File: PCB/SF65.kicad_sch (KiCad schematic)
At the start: 176 parts, among them J1 C165948_-_USB_C_Receptacle_US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, J2 SM02B-SRSS-TB(LF)(SN), Q1 Q_PMOS_GSD, SW1 CAP_STP, SW10 A, SW11 WIN_1.25U, SW12 2, SW13 W, SW14 S, SW15 Z, SW16 L_ALT_1.25U, SW17 L_ALT_1.5U, SW18 3, SW19 E, SW2 ESC, SW20 D, SW21 X, SW22 4, SW23 R, SW24 F, SW25 C, SW26 5, SW27 T, SW28 G, SW29 V, SW3 Tab, SW30 SPC_6.25U, SW31 SPC_7U, SW32 6, SW33 Y, SW34 H, SW35 B, SW36 7, SW37 U, SW38 J, SW39 N, SW4 CAP, SW40 8, SW41 I, SW42 K, SW43 M, SW44 R_ALT_1U, SW45 R_ALT_1.5U, SW46 9, SW47 O, SW48 L, SW49 ,, SW5 L_SHFT, SW50 R_WIN_1U, SW51 R_CTRL_1.5U, SW52 0, SW53 P, SW54 ;, SW55 ., SW56 R_CTRL_1U, SW57 -, SW58 [, SW59 ', SW6 L_CTRL_1.25U, SW60 /, SW61 =, SW62 ], SW63 R_SHFT_1.75U, SW64 LEFT, SW65 R_SHFT_1.5U, SW66 BCKSP, SW67 \, SW68 ENT, SW69 UP, SW7 L_CTRL_1.5U, SW70 DOWN, SW71 ENT_ISO, SW72 Tilde, SW73 Del, SW74 PG_UP, SW75 PG_DWN, SW76 RIGHT, SW8 1, SW9 Q, U1 TP4054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

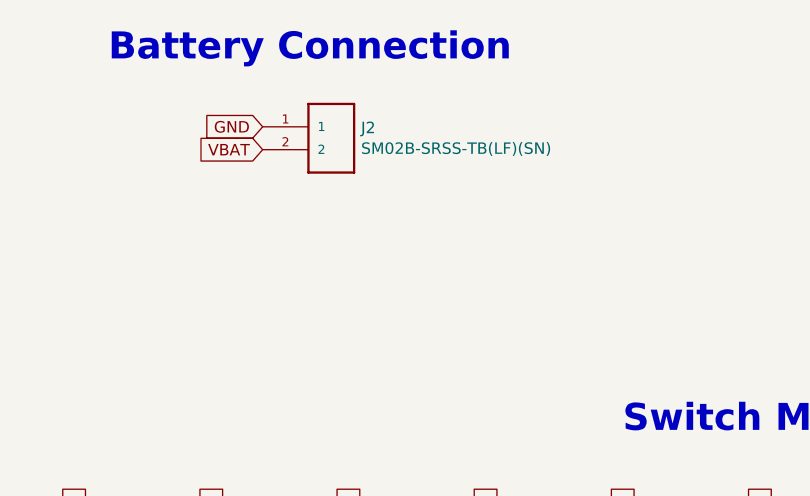
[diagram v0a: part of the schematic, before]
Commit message: working on routing, not complete
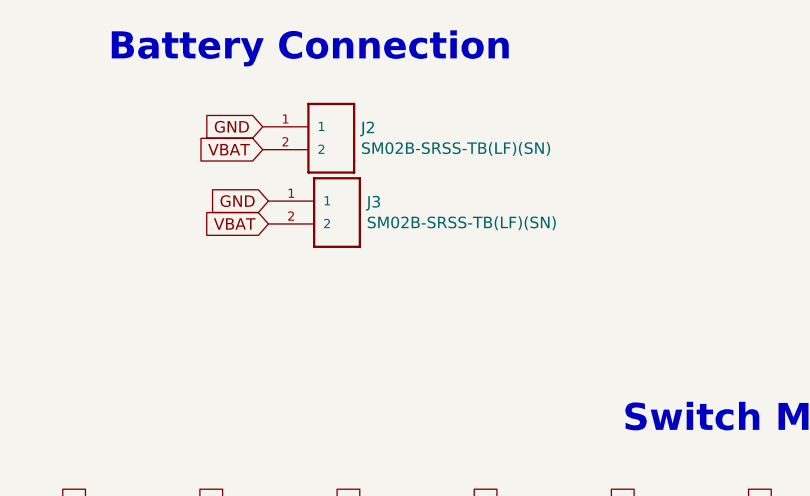
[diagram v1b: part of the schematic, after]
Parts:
- added J3: SM02B-SRSS-TB(LF)(SN), Connector_PinHeader_2.54mm:PinHeader_1x02_P2.54mm_Vertical, symbol SM02B-SRSS-TB_LF__SN_:SM02B-SRSS-TB(LF)(SN)
- H1, H2, H3, H4, H5, H6: footprint MountingHole:MountingHole_4.3mm_M4 -> MountingHole:MountingHole_2.2mm_M2
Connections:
- net GND: now also J3.1
- net VBAT: now also J3.2
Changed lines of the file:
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@@
+    (effects (font (size 1.27 1.27)) (justify right))
+  )
+  (global_label "GND" (shape input) (at 97.79 -5.08 180)    (property "Intersheet References" "${INTERSHEET_REFS}" (id 0) (at -396.24 -186.69 0)
+      (effects (font (size 1.27 1.27)) hide)
+    )
+    (effects (font (size 1.27 1.27)) (justify right))
+  )
+  (global_label "VBAT" (shape input) (at 97.79 -2.54 180)    (property "Intersheet References" "${INTERSHEET_REFS}" (id 0) (at -396.24 -181.61 0)
+      (effects (font (size 1.27 1.27)) hide)
+    )
     (effects (font (size 1.27 1.27)) (justify right))
   )
@@
       (effects (font (size 1.27 1.27)) (justify left))
     )
-    (property "Footprint" "MountingHole:MountingHole_4.3mm_M4" (id 2) (at -31.75 59.69 0)
+    (property "Footprint" "MountingHole:MountingHole_2.2mm_M2" (id 2) (at -31.75 59.69 0)
       (effects (font (size 1.27 1.27)) hide)
     )
@@
       (effects (font (size 1.27 1.27)) (justify left))
     )
-    (property "Footprint" "MountingHole:MountingHole_4.3mm_M4" (id 2) (at -31.75 67.31 0)
+    (property "Footprint" "MountingHole:MountingHole_2.2mm_M2" (id 2) (at -31.75 67.31 0)
       (effects (font (size 1.27 1.27)) hide)
     )
@@
       (effects (font (size 1.27 1.27)) (justify left))
     )
-    (property "Footprint" "MountingHole:MountingHole_4.3mm_M4" (id 2) (at -31.75 74.93 0)
+    (property "Footprint" "MountingHole:MountingHole_2.2mm_M2" (id 2) (at -31.75 74.93 0)
       (effects (font (size 1.27 1.27)) hide)
     )
@@
       (effects (font (size 1.27 1.27)) (justify left))
     )
-    (property "Footprint" "MountingHole:MountingHole_4.3mm_M4" (id 2) (at -31.75 82.55 0)
+    (property "Footprint" "MountingHole:MountingHole_2.2mm_M2" (id 2) (at -31.75 82.55 0)
       (effects (font (size 1.27 1.27)) hide)
     )
@@
       (effects (font (size 1.27 1.27)) (justify left))
     )
-    (property "Footprint" "MountingHole:MountingHole_4.3mm_M4" (id 2) (at -31.75 90.17 0)
+    (property "Footprint" "MountingHole:MountingHole_2.2mm_M2" (id 2) (at -31.75 90.17 0)
       (effects (font (size 1.27 1.27)) hide)
     )
@@
       (effects (font (size 1.27 1.27)) (justify left))
     )
-    (property "Footprint" "MountingHole:MountingHole_4.3mm_M4" (id 2) (at -31.75 97.79 0)
+    (property "Footprint" "MountingHole:MountingHole_2.2mm_M2" (id 2) (at -31.75 97.79 0)
       (effects (font (size 1.27 1.27)) hide)
     )
@@
     )
   )
+  (symbol (lib_id "SM02B-SRSS-TB_LF__SN_:SM02B-SRSS-TB(LF)(SN)") (at 97.79 0 0) (unit 1)
+    (in_bom yes) (on_board yes)
+    (property "Reference" "J3" (id 0) (at 108.7121 -4.9594 0)
+      (effects (font (size 1.27 1.27)) (justify left))
+    )
+    (property "Value" "SM02B-SRSS-TB(LF)(SN)" (id 1) (at 108.7121 -2.6607 0)
+      (effects (font (size 1.27 1.27)) (justify left))
+    )
+    (property "Footprint" "Connector_PinHeader_2.54mm:PinHeader_1x02_P2.54mm_Vertical" (id 2) (at 97.79 0 0)
+      (effects (font (size 1.27 1.27)) (justify left bottom) hide)
+    )
+    (property "Datasheet" "" (id 3) (at 97.79 0 0)
+      (effects (font (size 1.27 1.27)) (justify left bottom) hide)
+    )
+    (property "MP" "SM02B-SRSS-TB_LF__SN_" (id 4) (at 97.79 0 0)
+      (effects (font (size 1.27 1.27)) (justify left bottom) hide)
+    )
+    (property "AVAILABILITY" "Good" (id 5) (at 97.79 0 0)
+      (effects (font (size 1.27 1.27)) (justify left bottom) hide)
+    )
+    (property "PRICE" "0.23 USD" (id 6) (at 97.79 0 0)
+      (effects (font (size 1.27 1.27)) (justify left bottom) hide)
+    )
+    (property "DESCRIPTION" "SH Series 2 Position 1 mm Pitch Surface Mount Side Entry Shrouded Header" (id 7) (at 97.79 0 0)
+      (effects (font (size 1.27 1.27)) (justify left bottom) hide)
+    )
+    (property "MF" "JST" (id 8) (at 97.79 0 0)
+      (effects (font (size 1.27 1.27)) (justify left bottom) hide)
+    )
+    (property "PACKAGE" "None" (id 9) (at 97.79 0 0)
+      (effects (font (size 1.27 1.27)) (justify left bottom) hide)
+    )
+  )
   (symbol (lib_id "COBoards:Q_PMOS_GSD") (at -67.31 208.28 0) (unit 1)
     (in_bom yes) (on_board yes)
@@
     )
     (path "/57c2b6d5-409c-411a-87d5-01c7b443a274"
-      (reference "H1") (unit 1) (value "MountingHole_Pad") (footprint "MountingHole:MountingHole_4.3mm_M4")
+      (reference "H1") (unit 1) (value "MountingHole_Pad") (footprint "MountingHole:MountingHole_2.2mm_M2")
     )
     (path "/e5cfd2fa-2e8d-4059-88e3-68afbd63f1ed"
-      (reference "H2") (unit 1) (value "MountingHole_Pad") (footprint "MountingHole:MountingHole_4.3mm_M4")
+      (reference "H2") (unit 1) (value "MountingHole_Pad") (footprint "MountingHole:MountingHole_2.2mm_M2")
     )
     (path "/7f6e663e-0905-4ac2-9f94-84e0580516c6"
-      (reference "H3") (unit 1) (value "MountingHole_Pad") (footprint "MountingHole:MountingHole_4.3mm_M4")
+      (reference "H3") (unit 1) (value "MountingHole_Pad") (footprint "MountingHole:MountingHole_2.2mm_M2")
     )
     (path "/37c9d4f3-312f-47f1-9f4d-1c07624f0e6c"
-      (reference "H4") (unit 1) (value "MountingHole_Pad") (footprint "MountingHole:MountingHole_4.3mm_M4")
+      (reference "H4") (unit 1) (value "MountingHole_Pad") (footprint "MountingHole:MountingHole_2.2mm_M2")
     )
     (path "/b5d95a24-2753-4eb3-a390-07ddb53afbc0"
-      (reference "H5") (unit 1) (value "MountingHole_Pad") (footprint "MountingHole:MountingHole_4.3mm_M4")
+      (reference "H5") (unit 1) (value "MountingHole_Pad") (footprint "MountingHole:MountingHole_2.2mm_M2")
     )
     (path "/56d59270-8362-4bcd-b006-3b599e0c3d78"
-      (reference "H6") (unit 1) (value "MountingHole_Pad") (footprint "MountingHole:MountingHole_4.3mm_M4")
+      (reference "H6") (unit 1) (value "MountingHole_Pad") (footprint "MountingHole:MountingHole_2.2mm_M2")
     )
     (path "/828ef4a2-7b85-44c5-b8f5-7943f2969d3f"
@@
       (reference "J2") (unit 1) (value "SM02B-SRSS-TB(LF)(SN)") (footprint "COBoards:SM02B-SRSS-TB(LF)(SN)")
     )
+    (path "/70b5bca1-0b96-4ac4-a51e-5aa21489f7ca"
+      (reference "J3") (unit 1) (value "SM02B-SRSS-TB(LF)(SN)") (footprint "Connector_PinHeader_2.54mm:PinHeader_1x02_P2.54mm_Vertical")
+    )
     (path "/740890ae-c843-4a97-b564-35439ebfa574"

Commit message: about to swap in raytac module
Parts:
- added C6, C7: 15pF, Capacitor_SMD:C_0603_1608Metric, symbol Device:C_Small
- added U3: MDBT50Q-1MV2, RF_Module:Raytac_MDBT50Q, symbol RF_Module:MDBT50Q-1MV2
- added Y2: 32.768kHz, COBoards:FC-135R_L3.2-W1.5, symbol Device:Crystal
- C1, C2: value 22pF -> 15pF
- Y1: footprint Crystal:Crystal_SMD_MicroCrystal_CM9V-T1A-2Pin_1.6x1.0mm_HandSoldering -> COBoards:FC-135R_L3.2-W1.5
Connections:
- net BATTERY_MEASURE: now also U3.20 (P0.04/AIN2); no longer BLE1.3 (P0.03/AIN1_(LowFreq))
- net Col0: now also BLE1.2 (P1.10_(LowFreq)), U3.3 (P1.10)
- net Col1: now also BLE1.4 (P0.28/AIN4), U3.4 (P1.11)
- net Col10: now also U3.13 (P0.28/AIN4)
- net Col11: now also U3.14 (P0.30/AIN6)
- net Col12: now also U3.22 (P0.06)
- net Col13: now also U3.24 (P0.08)
- net Col14: now also U3.26 (TRACEDATA3/P1.09)
- net Col2: now also BLE1.6 (P1.13_(LowFreq)), U3.5 (P1.12)
- net Col3: now also U3.6 (P1.13)
- net Col4: now also U3.7 (P1.14)
- net Col5: now also U3.8 (P1.15)
- net Col6: now also U3.9 (P0.03/AIN1)
- net Col7: now also U3.10 (P0.29/AIN5)
- net Col8: now also U3.11 (P0.02/AIN0)
- net Col9: now also U3.12 (P0.31/AIN7)
- net D+: now also U3.35 (D+); no longer BLE1.31 (D+)
- net D-: now also U3.34 (D-); no longer BLE1.29 (D-)
- net GND: now also C6.1, C7.1; no longer BLE1.5 (GND)
- net P0.05: now also U3.50 (P1.02)
- net RESET: now also U3.40 (~RESET~/P0.18); no longer BLE1.26 (P0.18/RESET)
- net Row0: now also BLE1.1 (P1.11), U3.56 (P1.04)
- net Row1: now also U3.57 (P1.06)
- net Row2: now also U3.58 (P1.07)
- net Row3: now also U3.59 (P1.05)
- net Row4: now also U3.60 (P1.03)
- net SWC: now also U3.53 (SWDCLK); no longer BLE1.39 (SWDCLK)
- net SWD: now also U3.51 (SWDIO); no longer BLE1.37 (SWDIO)
- net VBUS: now also U3.32 (VBUS); no longer BLE1.27 (VBUS)
- new net: U3.1 (GND), U3.15 (GND), U3.2 (GND), U3.33 (GND), U3.55 (GND)
- new net: C6.2, U3.17 (XL1/P0.00), Y2.1
- new net: C7.2, U3.18 (XL2/P0.01), Y2.2
- no-connect marks 17 -> 7
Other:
- moved on the sheet: BATT1, BLE1, C1, C2, C3, C5, D1, D2, Q1, R5, R7, RESET1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

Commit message: order SF65 samples from JLC
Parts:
- removed BLE1: E73-2G4M08S1C, COBoards:E73-2G4M08S1C, symbol COBoards:E73-2G4M08S1C
- removed SW65: R_SHFT_1.5U, Button_Switch_Keyboard:SW_Cherry_MX_1.50u_PCB, symbol Switch:SW_Push
- removed Y1: 32.768kHz, COBoards:FC-135R_L3.2-W1.5, symbol Device:Crystal
- added D72: D, Diode_SMD:D_SOD-123, symbol Device:D_Small
- added H10, H11, H7, H8, H9: MountingHole_Pad, MountingHole:MountingHole_4.3mm_M4, symbol Mechanical:MountingHole_Pad
- added R10, R9: 27R, Resistor_SMD:R_0603_1608Metric, symbol Device:R_Small
- added R11: 1M, Resistor_SMD:R_0603_1608Metric, symbol Device:R_Small
- added SW77: ISO_SPARE, Button_Switch_Keyboard:SW_Cherry_MX_1.00u_PCB, symbol Switch:SW_Push
- added TP1, TP2, TP3: TestPoint, TestPoint:TestPoint_Pad_1.0x1.0mm, symbol Connector:TestPoint
- added U4: USBLC6-2SC6, Package_TO_SOT_SMD:SOT-23-6, symbol Power_Protection:USBLC6-2SC6
- C1: value 15pF -> 10uF
- C2: value 15pF -> 4.7nF
- C3: value 4.7uF -> 10uF
- C5: value 10uF -> 1uF
- D1, D3: footprint LED_SMD:LED_0603_1608Metric_Pad1.05x0.95mm_HandSolder -> LED_SMD:LED_0603_1608Metric
- D2: footprint Diode_SMD:D_SOD-323_HandSoldering -> Diode_SMD:D_SOD-323
- H1, H6: footprint MountingHole:MountingHole_2.2mm_M2 -> MountingHole:MountingHole_4.3mm_M4
- J1: symbol COBoards:C165948_-_USB_C_Receptacle_USB2.0_SMD -> Connector:USB_C_Receptacle_USB2.0
- R1, R2, R3, R4, R5, R6, R7, R8: footprint Resistor_SMD:R_0603_1608Metric_Pad0.98x0.95mm_HandSolder -> Resistor_SMD:R_0603_1608Metric
- renumbered Y2 to Y1
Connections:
- net BATTERY_MEASURE: now also U3.36 (P0.14); no longer U3.20 (P0.04/AIN2)
- net Col12: now also U3.23 (TRACECLK/P0.07), SW77.1; no longer U3.22 (P0.06)
- net Col13: now also U3.25 (P1.08); no longer U3.24 (P0.08)
- net Col14: now also U3.27 (TRACEDATA2/P0.11); no longer U3.26 (TRACEDATA3/P1.09)
- net D+: now also R10.1, U4.3 (I/O2); no longer J1.A6 (D+), J1.B6 (D+), U3.35 (D+)
- net D-: now also R9.1, U4.4 (I/O2); no longer J1.A7 (D-), J1.B7 (D-), U3.34 (D-)
- net GND: now also C3.1, U3.1 (GND), U3.15 (GND), U3.2 (GND), U3.33 (GND), U3.55 (GND), R11.1, U4.2 (GND); no longer C3.2
- net Row0: now also U3.60 (P1.03); no longer U3.56 (P1.04)
- net Row1: now also U3.59 (P1.05); no longer U3.57 (P1.06)
- net Row2: now also D72.1 (K)
- net Row3: now also U3.57 (P1.06); no longer U3.59 (P1.05)
- net Row4: now also U3.56 (P1.04); no longer U3.60 (P1.03)
- net VBUS: now also C3.2, U4.5 (VBUS)
- net VDD: now reaches C1.2
- net VDD: now also C5.1, U2.5 (VOUT), U3.28 (VDD), U3.30 (VDDH)
- net at C2.2: now also J1.S1 (SHIELD), R11.2
- net at U3.41 (P0.17): now also TP1.1
- net at U3.44 (P0.20): now also TP2.1
- net at U3.46 (P0.22): now also TP3.1
- net at D2.1 (K), Q1.2 (S), U2.1 (VIN)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: no longer C3.1
- removed net VDD_H: C5.1, SWD/C1.2 (Pin_2), U2.5 (VOUT)
- new net: D72.2 (A), SW77.2
- new net: R9.2, U3.34 (D-)
- new net: R10.2, U3.35 (D+)
- new net: J1.A6 (D+), J1.B6 (D+), U4.1 (I/O1)
- new net: J1.A7 (D-), J1.B7 (D-), U4.6 (I/O1)
- no-connect marks 7 -> 37
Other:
- note added: "Battery Charger"
- note added: "Power In"
- note removed: "BLE Module"
- note removed: "LiPo Charger"
- note removed: "Power & Filtering"
- company: (none) -> CO Boards
- title: (none) -> SP56
- moved on the sheet: BATT1, C4, C6, C7, D1, D2, D3, H2, H3, H4, H5, J2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

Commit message: starting to make v2 edits, not finished
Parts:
- removed SWD/C1: Conn_01x04_Female, Connector_PinHeader_2.54mm:PinHeader_1x04_P2.54mm_Vertical, symbol Connector:Conn_01x04_Female
- added J4: Conn_ARM_JTAG_SWD_10, Connector:Tag-Connect_TC2030-IDC-NL_2x03_P1.27mm_Vertical, symbol Connector:Conn_ARM_JTAG_SWD_10
- added SW65: Rotary_Encoder_Switch-Device-SofleKeyboard-rescue, symbol COBoards:Rotary_Encoder_Switch-Device-SofleKeyboard-rescue
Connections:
- net BATTERY_MEASURE: now also U3.20 (P0.04/AIN2); no longer U3.36 (P0.14)
- net Col12: now also U3.22 (P0.06); no longer U3.23 (TRACECLK/P0.07)
- net Col13: now also U3.24 (P0.08); no longer U3.25 (P1.08)
- net Col14: now also U3.26 (TRACEDATA3/P1.09); no longer U3.27 (TRACEDATA2/P0.11)
- net D+: now also U4.1 (I/O1); no longer U4.3 (I/O2)
- net D-: now also U4.3 (I/O2); no longer U4.4 (I/O2)
- net GND: now also J4.3 (GND), J4.5 (GND), J4.9 (GNDDetect)
- net RESET: now also J4.10 (~RESET~)
- net SWC: now also J4.4 (SWDCLK/TCK)
- net SWD: now also J4.2 (SWDIO/TMS)
- net VDD: now also J4.1 (VTref)
- net at J1.A6 (D+), J1.B6 (D+): now also U4.6 (I/O1); no longer U4.1 (I/O1)
- net at J1.A7 (D-), J1.B7 (D-): now also U4.4 (I/O2); no longer U4.6 (I/O1)
- net P0.05 renamed BOOT_LED
- no-connect marks 37 -> 34
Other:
- moved on the sheet: U4
